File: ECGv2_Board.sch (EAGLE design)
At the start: 38 parts, among them IC1 LF347D, IC2 LF347D, IC3 TINY15LS, Q1 BSS84

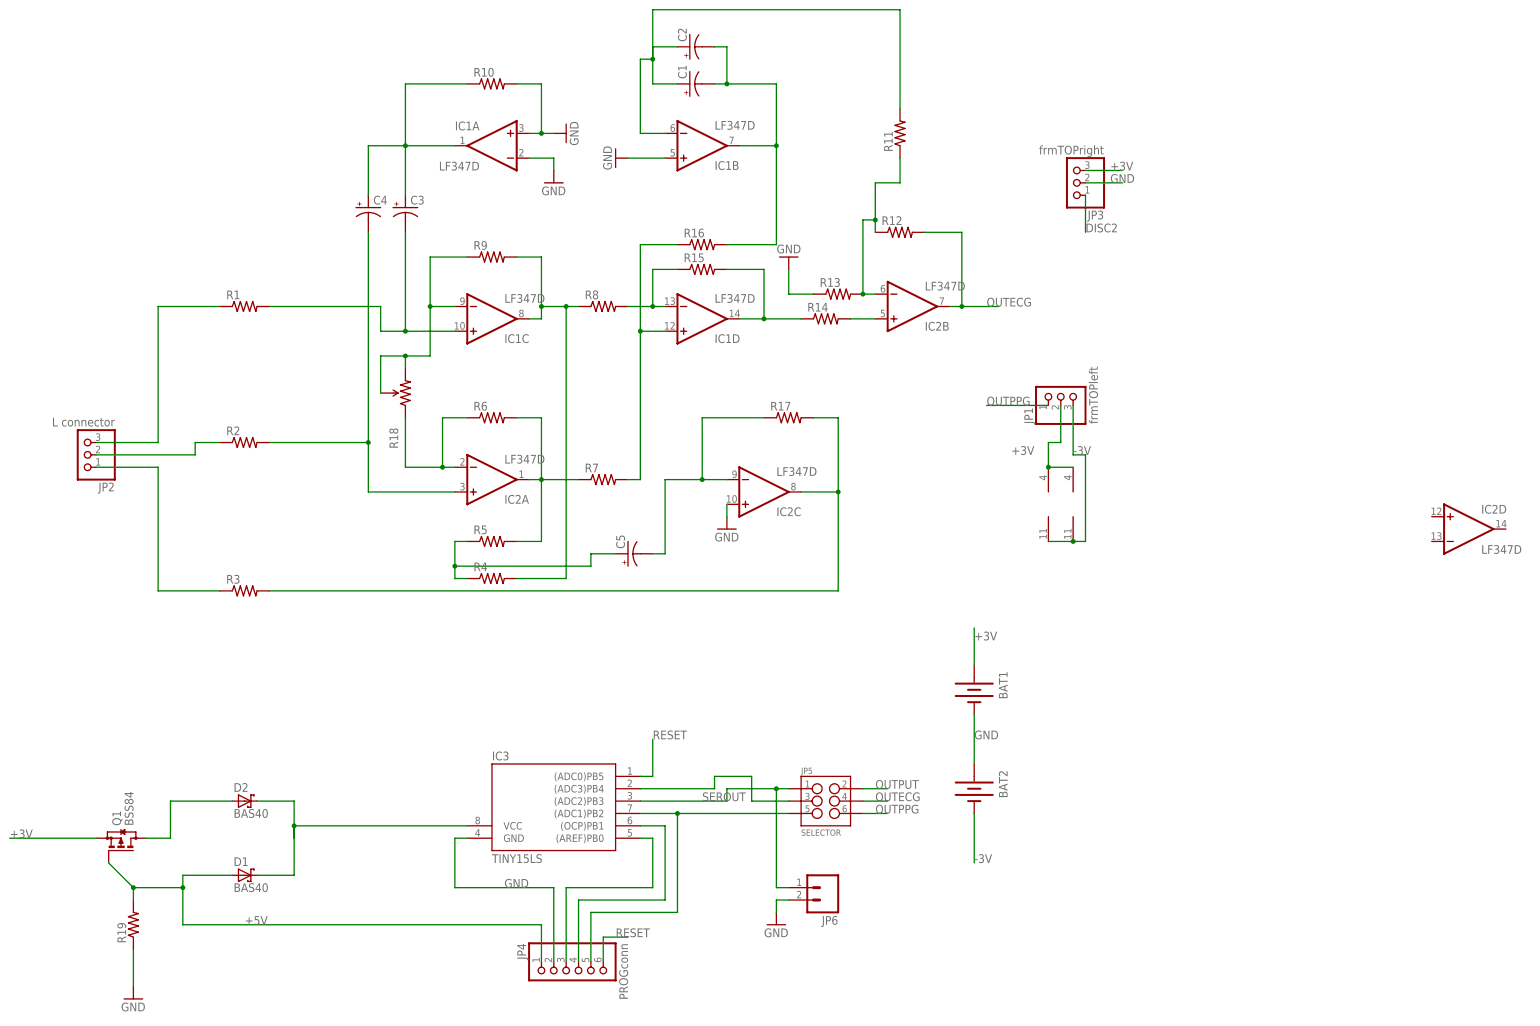
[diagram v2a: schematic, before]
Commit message: -restructuring
-identification and restructuring of circuit
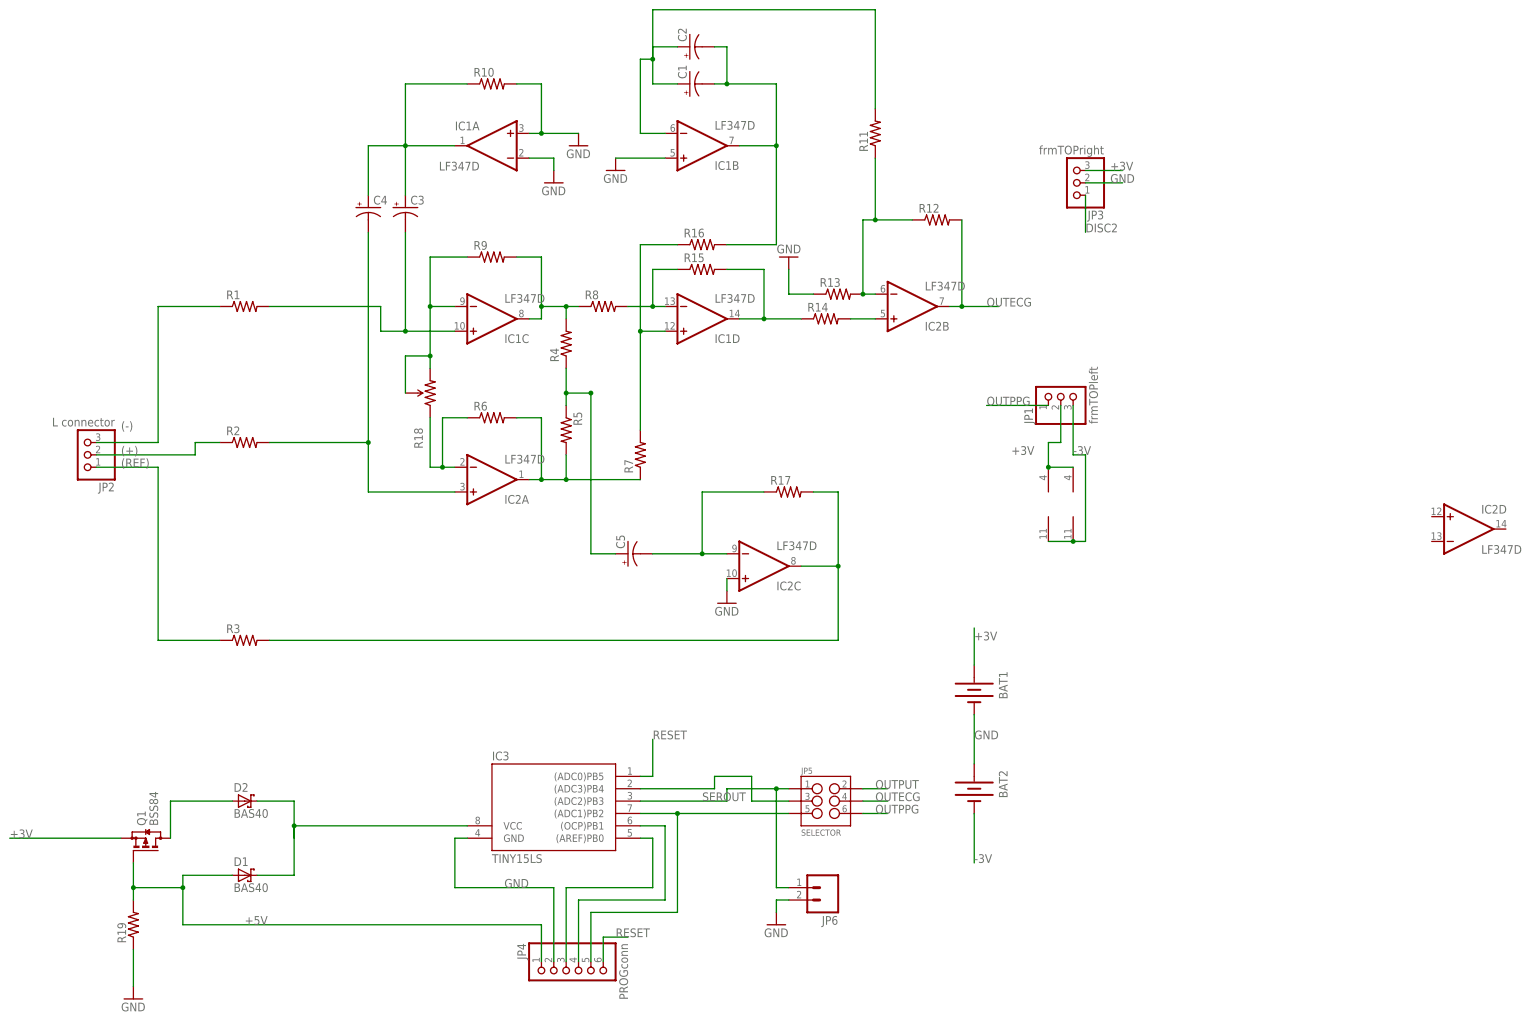
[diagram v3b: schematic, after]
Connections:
- net N$20 renamed (-)
- net N$21 renamed (+)
- net N$22 renamed (REF)
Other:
- moved on the sheet: IC2C, Q1, R11, R12, R17, R18, R3, R4, R5, R7
